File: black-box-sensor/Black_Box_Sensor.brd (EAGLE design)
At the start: 37.2 x 44 mm, 56 parts, among them J1 104031-0811, J2 UX60-MB-5S8, J3 B4B-PH-SM4-TBT(LF)(SN), U1 ADXL375, U2 ADXL375, U3 ATMEGA32U4-AU, U4 FXAS21002CQR1, U6 NL27WZ32USG, U7 LT1129CST-5#PBF, U8 AD8426ACPZ-WP, U9 TXU0304

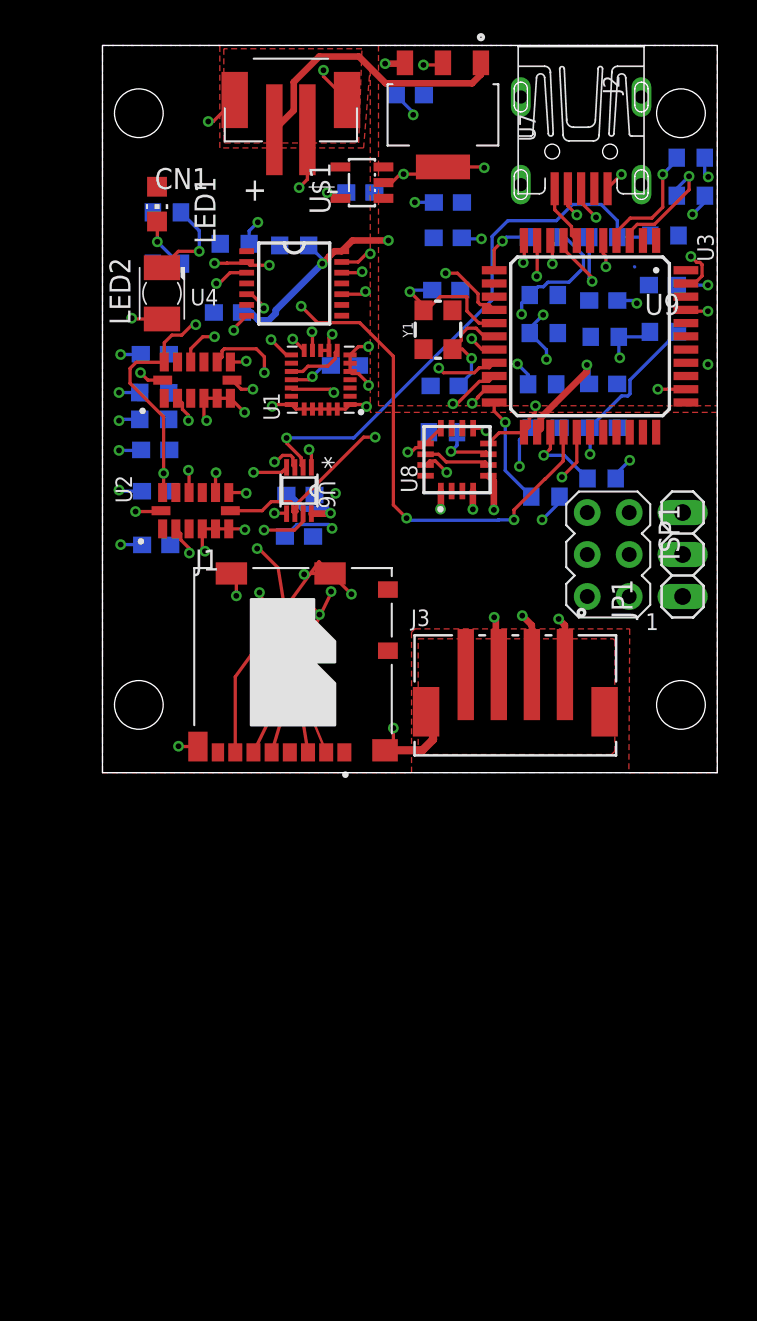
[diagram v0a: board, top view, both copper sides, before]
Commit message: NOTE: ATMega needs 7V, not 5V. Need another voltage regulator, probably need to remove diodes
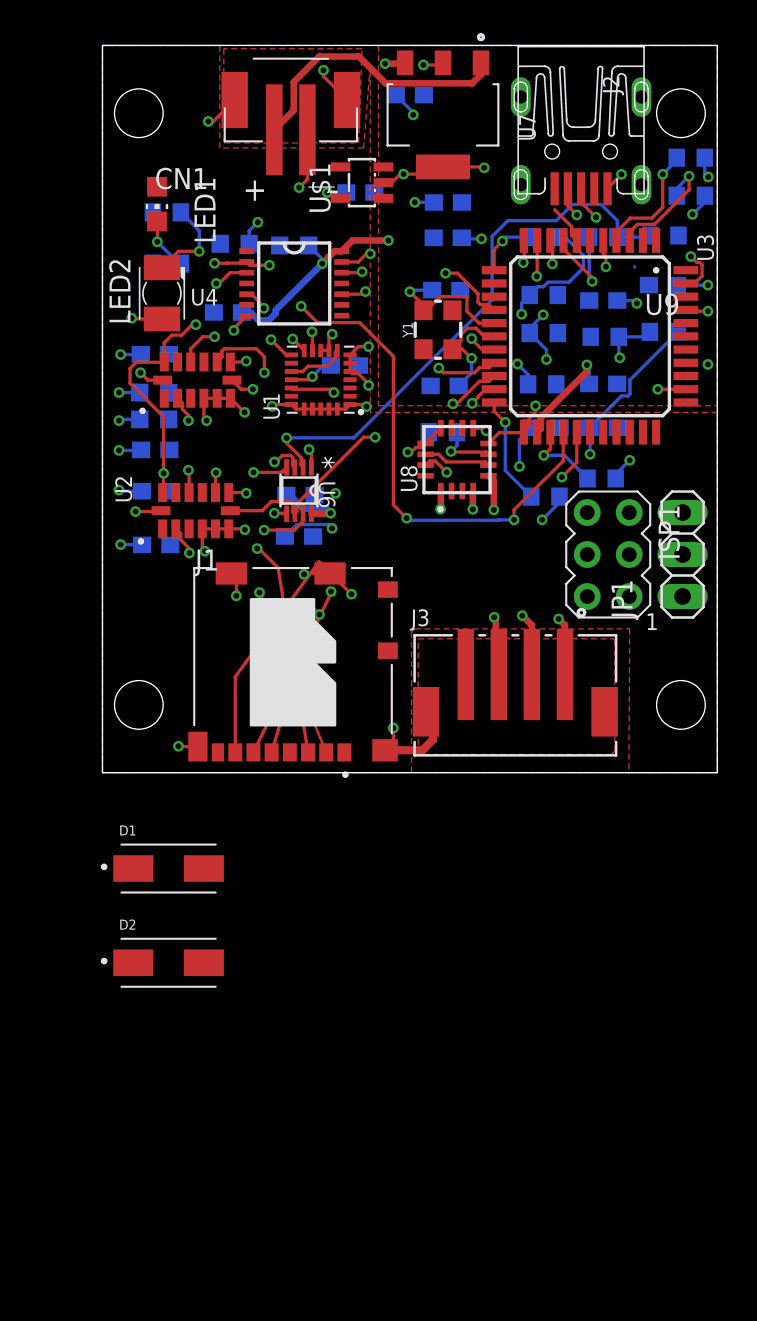
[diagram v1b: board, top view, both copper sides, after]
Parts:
- added D1, D2: CDBA240LL-HF, BBS_Library:DIOM5225X250N
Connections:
- new net N$9: D2.A, ISP1.2
- net +5V: now also D1.C, D2.C; no longer ISP1.2
- net VBUS: now also D1.A
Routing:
- net GND: track 83.9 -> 82.6 mm
- net VBUS: track 3.69 -> 2.42 mm
- net +5V: track 53.0 -> 51.9 mm
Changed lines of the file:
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@@
 <attribute name="VOLTAGE" value="10V" x="15.6" y="35.1" size="1.778" layer="28" rot="MR180" display="off"/>
+</element>
+<element name="D1" library="BBS_Library" package="DIOM5225X250N" value="CDBA240LL-HF" x="4" y="-5.8" smashed="yes">
+<attribute name="DKPN" value="641-1698-1-ND" x="4" y="-5.8" size="1.778" layer="27" display="off"/>
+<attribute name="NAME" x="1" y="-3.8" size="0.6096" layer="25" font="vector" ratio="10"/>
+<attribute name="VALUE" x="1" y="-7.8" size="0.6096" layer="27" font="vector" ratio="10" align="top-left"/>
+</element>
+<element name="D2" library="BBS_Library" package="DIOM5225X250N" value="CDBA240LL-HF" x="4" y="-11.5" smashed="yes">
+<attribute name="DKPN" value="641-1698-1-ND" x="4" y="-11.5" size="1.778" layer="27" display="off"/>
+<attribute name="NAME" x="1" y="-9.5" size="0.6096" layer="25" font="vector" ratio="10"/>
+<attribute name="VALUE" x="1" y="-13.5" size="0.6096" layer="27" font="vector" ratio="10" align="top-left"/>
 </element>
 </elements>
@@
 <contactref element="C18" pad="2"/>
 <contactref element="R4" pad="1"/>
-<contactref element="J3" pad="5"/>
-<contactref element="J3" pad="6"/>
 <contactref element="J3" pad="4"/>
 <polygon width="0.2" layer="16" thermals="no">
@@
 <wire x1="8.1" y1="11.703653125" x2="8.0612125" y2="11.714103125" width="0.2" layer="1"/>
 <via x="8.1" y="10.7" extent="1-16" drill="0.35"/>
-<wire x1="30.38" y1="3.6852" x2="30.38" y2="2.98" width="0.2" layer="1"/>
 <wire x1="17.095" y1="1.355" x2="17.6" y2="1.355" width="0.2" layer="1"/>
 <wire x1="17.6" y1="1.355" x2="17.6" y2="2.7" width="0.2" layer="1"/>
@@
 <wire x1="19.355" y1="1.355" x2="20" y2="2" width="0.5" layer="1"/>
 <wire x1="20" y1="2" x2="20" y2="3.2652" width="0.5" layer="1"/>
-<wire x1="20" y1="3.2652" x2="19.58" y2="3.6852" width="0.5" layer="1"/>
+<contactref element="J3" pad="5"/>
+<contactref element="J3" pad="6"/>
 <wire x1="35.6" y1="31.2314" x2="34.85" y2="32.5" width="0" layer="19" extent="16-16"/>
 <wire x1="33.06" y1="29.5" x2="35.3" y2="29.6" width="0" layer="19" extent="1-16"/>
@@
 <wire x1="4.1" y1="13.78" x2="4.44" y2="14.7525" width="0" layer="19" extent="1-16"/>
 <wire x1="7.8" y1="12.055" x2="6.2" y2="13.4" width="0" layer="19" extent="1-1"/>
-<wire x1="17.6" y1="2.7" x2="8.0612125" y2="11.714103125" width="0" layer="19" extent="1-1"/>
-<wire x1="21.98" y1="5.9352" x2="19.58" y2="3.6852" width="0" layer="19" extent="1-1"/>
 <wire x1="9.1388" y1="18.1694" x2="8.614975" y2="14.7" width="0" layer="19" extent="1-1"/>
 <wire x1="12.83" y1="16.8" x2="11.14" y2="18.47" width="0" layer="19" extent="1-16"/>
 <wire x1="12.74" y1="14.29" x2="12.83" y2="16.8" width="0" layer="19" extent="16-16"/>
-<wire x1="13.77" y1="12.055" x2="12.74" y2="14.29" width="0" layer="19" extent="1-16"/>
+<wire x1="12.2" y1="12" x2="12.74" y2="14.29" width="0" layer="19" extent="16-16"/>
 <wire x1="13.83" y1="10.96" x2="13.77" y2="12.055" width="0" layer="19" extent="1-1"/>
 <wire x1="5.775" y1="1.58" x2="9.135" y2="1.23" width="0" layer="19" extent="1-1"/>
@@
 <wire x1="29.33" y1="15.74" x2="27.66" y2="20.87" width="0" layer="19" extent="16-16"/>
 <wire x1="35.1" y1="15.74" x2="29.33" y2="15.74" width="0" layer="19" extent="1-1"/>
+<wire x1="17.095" y1="1.355" x2="9.135" y2="1.23" width="0" layer="19" extent="1-1"/>
+<wire x1="19.58" y1="3.6852" x2="20" y2="3.2652" width="0" layer="19" extent="1-1"/>
+<wire x1="21.98" y1="5.9352" x2="19.58" y2="3.6852" width="0" layer="19" extent="1-1"/>
 <wire x1="30.38" y1="3.6852" x2="21.98" y2="5.9352" width="0" layer="19" extent="1-1"/>
 </signal>
@@
 </signal>
 <signal name="VBUS">
-<contactref element="J2" pad="5"/>
 <contactref element="U3" pad="7"/>
 <wire x1="28.377" y1="33.044025" x2="28.377" y2="32.523" width="0.2" layer="1"/>
 <wire x1="28.377" y1="32.523" x2="28.7" y2="32.2" width="0.2" layer="1"/>
-<wire x1="27.36" y1="35.33" x2="27.36" y2="34.061025" width="0.2" layer="1"/>
 <wire x1="27.36" y1="34.061025" x2="28.377" y2="33.044025" width="0.2" layer="1"/>
+<contactref element="J2" pad="5"/>
+<contactref element="D1" pad="A"/>
+<wire x1="27.36" y1="35.33" x2="27.36" y2="34.061025" width="0" layer="19" extent="1-1"/>
+<wire x1="6.135" y1="-5.8" x2="28.7" y2="32.2" width="0" layer="19" extent="1-1"/>
 </signal>
 <signal name="CS4">
@@
 <contactref element="C13" pad="1"/>
 <contactref element="C14" pad="1"/>
-<contactref element="ISP1" pad="2"/>
 <contactref element="JP1" pad="1"/>
 <contactref element="C21" pad="1"/>
@@
 <via x="29.31" y="24.67" extent="1-16" drill="0.35"/>
 <wire x1="31.45495625" y1="11.662" x2="32.28504375" y2="11.662" width="0.4" layer="2"/>
-<wire x1="29.33" y1="10.66" x2="30.45295625" y2="10.66" width="0.4" layer="2"/>
 <wire x1="33.28704375" y1="10.66" x2="35.1" y2="10.66" width="0.4" layer="2"/>
 <wire x1="30.45295625" y1="10.66" x2="31.45495625" y2="11.662" width="0.4" layer="2"/>
@@
 <wire x1="20.04" y1="34.51" x2="18.9" y2="34.51" width="0.2" layer="16"/>
 <via x="18.9" y="34.51" extent="1-16" drill="0.35"/>
+<contactref element="D1" pad="C"/>
+<contactref element="D2" pad="C"/>
+<wire x1="34.76" y1="29.5" x2="35.3" y2="30.4" width="0" layer="19" extent="1-16"/>
+<wire x1="32.33" y1="28.4" x2="34.76" y2="29.5" width="0" layer="19" extent="16-16"/>
 <wire x1="29.5" y1="32.2" x2="31.15" y2="28.57" width="0" layer="19" extent="1-16"/>
+<wire x1="29.31" y1="24.67" x2="31.15" y2="28.57" width="0" layer="19" extent="16-16"/>
+<wire x1="36.6314" y1="24.7" x2="36.6314" y2="29.5" width="0" layer="19" extent="1-1"/>
+<wire x1="35.3" y1="22.4" x2="36.6314" y2="24.7" width="0" layer="19" extent="1-1"/>
+<wire x1="23.7" y1="29.6" x2="29.5" y2="32.2" width="0" layer="19" extent="1-1"/>
+<wire x1="23.7" y1="28.8" x2="23.7" y2="29.6" width="0" layer="19" extent="1-1"/>
+<wire x1="22.93" y1="32.3" x2="23.7" y2="29.6" width="0" layer="19" extent="1-1"/>
+<wire x1="20.05" y1="34.5" x2="21.74" y2="32.36" width="0" layer="19" extent="16-16"/>
+<wire x1="17" y1="34.75" x2="18.9" y2="34.51" width="0" layer="19" extent="1-1"/>
+<wire x1="17" y1="36.65" x2="17" y2="34.75" width="0" layer="19" extent="1-1"/>
+<wire x1="17.3" y1="32.2" x2="17" y2="34.75" width="0" layer="19" extent="1-1"/>
+<wire x1="18.8" y1="39.8" x2="17" y2="36.65" width="0" layer="19" extent="1-1"/>
+<wire x1="18.3013" y1="42.9496" x2="18.2894" y2="42.9377" width="0" layer="19" extent="1-1"/>
+<wire x1="1.865" y1="-5.8" x2="30.45295625" y2="10.66" width="0" layer="19" extent="1-2"/>
+<wire x1="1.865" y1="-11.5" x2="1.865" y2="-5.8" width="0" layer="19" extent="1-1"/>
 </signal>
 <signal name="MISO_5V">
@@
 <contactref element="U9" pad="8"/>
 </signal>
+<signal name="N$9">
+<contactref element="ISP1" pad="2"/>
+<contactref element="D2" pad="A"/>
+<wire x1="6.135" y1="-11.5" x2="29.33" y2="10.66" width="0" layer="19" extent="1-1"/>
+</signal>
 </signals>

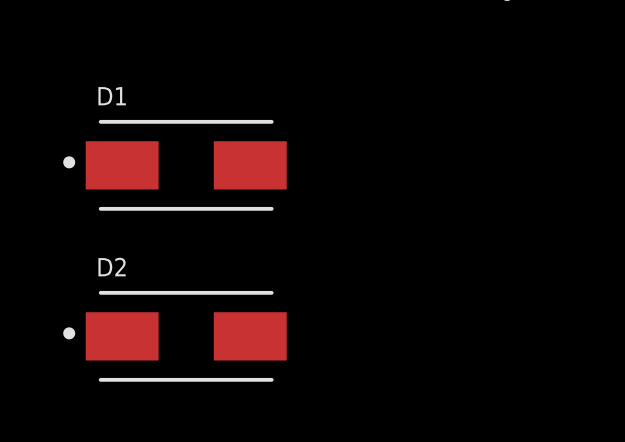
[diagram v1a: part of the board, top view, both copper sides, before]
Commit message: ATMega voltages correct, but capacitor values needed for Xtal
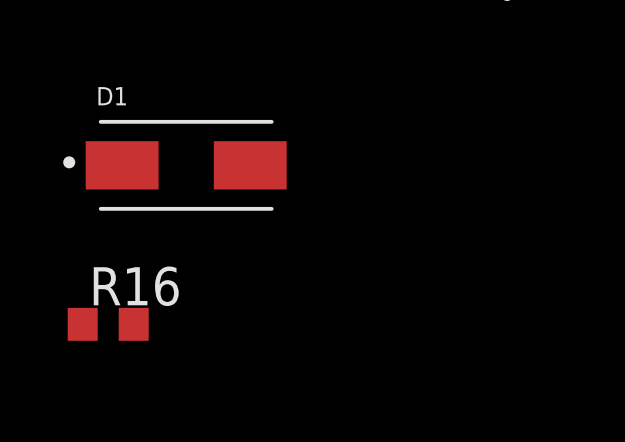
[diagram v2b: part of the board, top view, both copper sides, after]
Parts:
- removed D2: CDBA240LL-HF, BBS_Library:DIOM5225X250N
- added R16: 10k, rcl:R0603
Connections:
- net +5V: now also R16.2; no longer D2.C, U3.13
- net N$9: no longer D2.A
- net RST_5V: now also R16.1, U3.13
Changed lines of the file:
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@@
 <attribute name="VALUE" x="1" y="-7.8" size="0.6096" layer="27" font="vector" ratio="10" align="top-left"/>
 </element>
-<element name="D2" library="BBS_Library" package="DIOM5225X250N" value="CDBA240LL-HF" x="4" y="-11.5" smashed="yes">
-<attribute name="DKPN" value="641-1698-1-ND" x="4" y="-11.5" size="1.778" layer="27" display="off"/>
-<attribute name="NAME" x="1" y="-9.5" size="0.6096" layer="25" font="vector" ratio="10"/>
-<attribute name="VALUE" x="1" y="-13.5" size="0.6096" layer="27" font="vector" ratio="10" align="top-left"/>
+<element name="R16" library="rcl" library_urn="urn:adsk.eagle:library:334" package="R0603" package3d_urn="urn:adsk.eagle:package:23555/3" value="10k" x="1.4" y="-11.1" smashed="yes">
+<attribute name="NAME" x="0.765" y="-10.465" size="1.27" layer="25"/>
+<attribute name="POPULARITY" value="77" x="1.4" y="-11.1" size="1.778" layer="27" display="off"/>
+<attribute name="SPICEPREFIX" value="R" x="1.4" y="-11.1" size="1.778" layer="27" display="off"/>
+<attribute name="VALUE" x="0.765" y="-13.005" size="1.27" layer="27"/>
 </element>
 </elements>
@@
 </signal>
 <signal name="+5V">
-<contactref element="U3" pad="13"/>
 <contactref element="U3" pad="14"/>
 <contactref element="U3" pad="34"/>
@@
 <via x="18.9" y="34.51" extent="1-16" drill="0.35"/>
 <contactref element="D1" pad="C"/>
-<contactref element="D2" pad="C"/>
+<contactref element="R16" pad="2"/>
 <wire x1="34.76" y1="29.5" x2="35.3" y2="30.4" width="0" layer="19" extent="1-16"/>
 <wire x1="32.33" y1="28.4" x2="34.76" y2="29.5" width="0" layer="19" extent="16-16"/>
@@
 <wire x1="36.6314" y1="24.7" x2="36.6314" y2="29.5" width="0" layer="19" extent="1-1"/>
 <wire x1="35.3" y1="22.4" x2="36.6314" y2="24.7" width="0" layer="19" extent="1-1"/>
-<wire x1="23.7" y1="29.6" x2="29.5" y2="32.2" width="0" layer="19" extent="1-1"/>
-<wire x1="23.7" y1="28.8" x2="23.7" y2="29.6" width="0" layer="19" extent="1-1"/>
-<wire x1="22.93" y1="32.3" x2="23.7" y2="29.6" width="0" layer="19" extent="1-1"/>
+<wire x1="22.93" y1="32.3" x2="29.5" y2="32.2" width="0" layer="19" extent="1-1"/>
 <wire x1="20.05" y1="34.5" x2="21.74" y2="32.36" width="0" layer="19" extent="16-16"/>
 <wire x1="17" y1="34.75" x2="18.9" y2="34.51" width="0" layer="19" extent="1-1"/>
 <wire x1="17" y1="36.65" x2="17" y2="34.75" width="0" layer="19" extent="1-1"/>
 <wire x1="17.3" y1="32.2" x2="17" y2="34.75" width="0" layer="19" extent="1-1"/>
+<wire x1="23.7" y1="28.8" x2="22.93" y2="32.3" width="0" layer="19" extent="1-1"/>
 <wire x1="18.8" y1="39.8" x2="17" y2="36.65" width="0" layer="19" extent="1-1"/>
 <wire x1="18.3013" y1="42.9496" x2="18.2894" y2="42.9377" width="0" layer="19" extent="1-1"/>
 <wire x1="1.865" y1="-5.8" x2="30.45295625" y2="10.66" width="0" layer="19" extent="1-2"/>
-<wire x1="1.865" y1="-11.5" x2="1.865" y2="-5.8" width="0" layer="19" extent="1-1"/>
+<wire x1="2.25" y1="-11.1" x2="1.865" y2="-5.8" width="0" layer="19" extent="1-1"/>
 </signal>
 <signal name="MISO_5V">
@@
 <signal name="RST_5V">
 <contactref element="ISP1" pad="5"/>
+<contactref element="U3" pad="13"/>
+<contactref element="R16" pad="1"/>
+<wire x1="31.87" y1="15.74" x2="23.7" y2="29.6" width="0" layer="19" extent="1-1"/>
+<wire x1="0.55" y1="-11.1" x2="31.87" y2="15.74" width="0" layer="19" extent="1-1"/>
 </signal>
 <signal name="MOSI_5V">
@@
 <signal name="N$9">
 <contactref element="ISP1" pad="2"/>
-<contactref element="D2" pad="A"/>
-<wire x1="6.135" y1="-11.5" x2="29.33" y2="10.66" width="0" layer="19" extent="1-1"/>
 </signal>
 </signals>

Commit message: assign XTal cap values
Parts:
- C15, C20: value (none) -> 7.5pF
- C6: value 100nF -> 0.1uF
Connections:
- net +5V: now also C23.1; no longer C23.2
- net 3.3V: now also C22.1; no longer C22.2
- net GND: now also C22.2, C23.2; no longer C22.1, C23.1
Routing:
- net 3.3V: track 48.0 -> 46.5 mm, vias 14 -> 13
- net N$7: track 8.73 -> 7.35 mm
- net VBUS: track 2.42 -> 3.69 mm
- net +5V: track 51.9 -> 50.7 mm

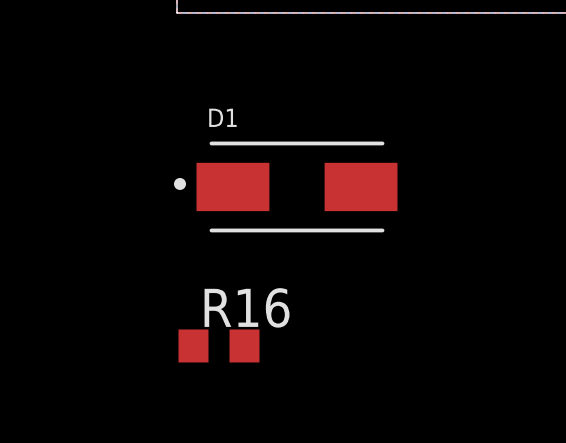
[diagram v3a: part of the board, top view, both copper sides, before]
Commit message: Gyroscope added to schematic
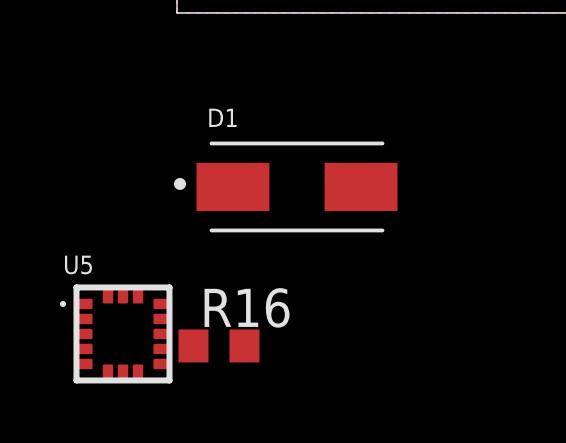
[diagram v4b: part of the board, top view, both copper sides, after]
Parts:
- added U5: IAM-20380, BBS_Library:PQFN50P300X300X80-16N
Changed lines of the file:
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@@
 <attribute name="VALUE" x="0.765" y="-13.005" size="1.27" layer="27"/>
+</element>
+<element name="U5" library="BBS_Library" package="PQFN50P300X300X80-16N" value="IAM-20380" x="-1.8" y="-10.7" smashed="yes">
+<attribute name="DKPN" value="1428-1153-2-ND" x="-1.8" y="-10.7" size="1.778" layer="27" display="off"/>
+<attribute name="NAME" x="-3.8" y="-8.7" size="0.6107375" layer="25" font="vector" ratio="10"/>
+<attribute name="VALUE" x="-3.8" y="-12.7" size="0.609659375" layer="27" font="vector" ratio="10" align="top-left"/>
 </element>
 </elements>
